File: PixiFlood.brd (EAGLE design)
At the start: 32 x 47.2 mm, 60 parts, among them IC1 74LVC1G125DBV, IC2 WS2811SOP8, IC3 BD9G401EFJ-ME2, IC4 AL-8861SOT89-5, IC5 AL-8861SOT89-5, IC6 AL-8861SOT89-5, Q1 BC847BC847, Q2 BC847BC847, Q3 BC847BC847

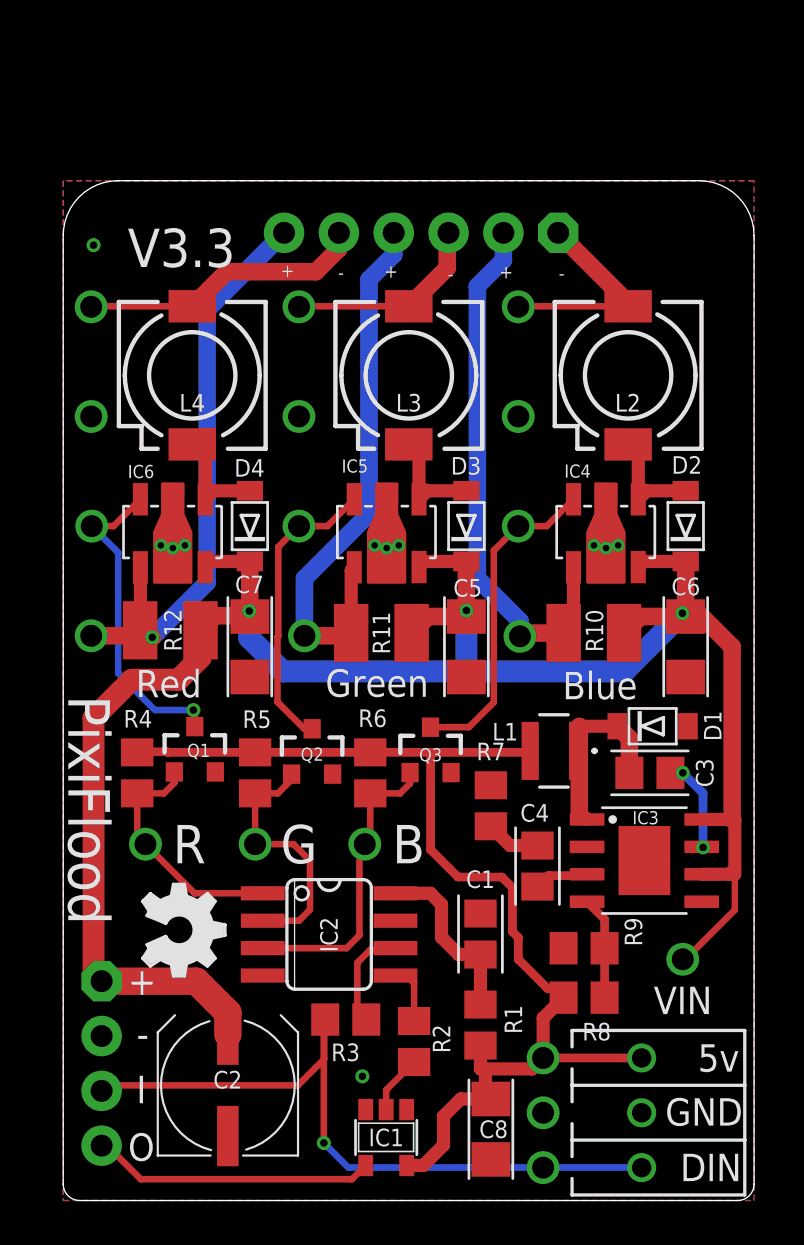
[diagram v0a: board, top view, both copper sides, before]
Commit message: Cleaned up some labels
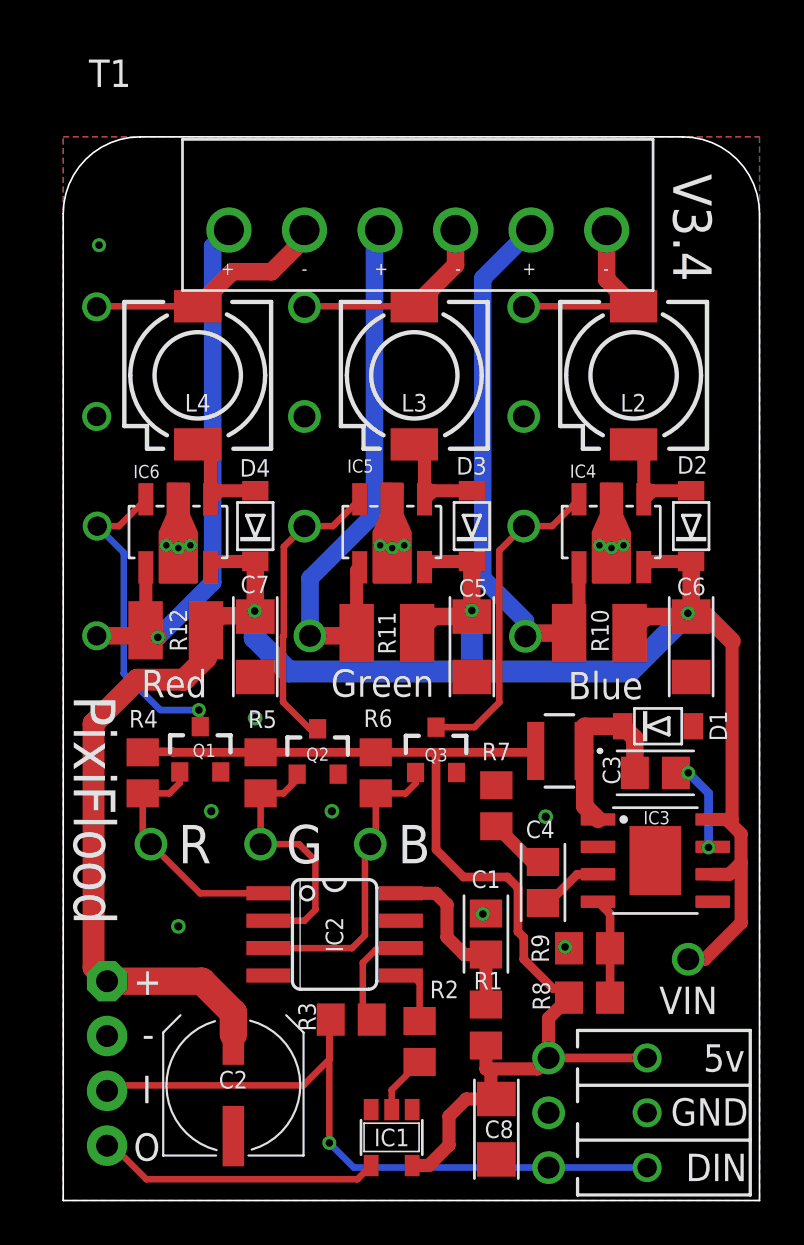
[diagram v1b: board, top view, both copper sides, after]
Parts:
- removed HDR3: (no value), headers:1X06
- added T1: ST06ECH350V-06P, connectors:ECH350V-06P
- LOGO: device ohw-logo:OSHW_FILLX150_NOTEXT -> ohw-logo:OSHW_FILLX200_NOTEXT
- TP1, TP14, TP4, TP9: device headers:TP-2 -> headers:TP-1
- moved LOGO 4.20 mm to (7.88, 10.3), turned to 0 degrees
- moved C4 0.80 mm to (22.2, 14.7)
- moved IC3 0.51 mm to (27.4, 15.7)
- moved C1 0.25 mm to (19.6, 12.3)
- moved C5 0.25 mm to (18.9, 25.7)
- moved C6 0.25 mm to (29.1, 25.7)
- moved D1 0.25 mm to (27.6, 22.0)
- moved D2 0.25 mm to (29.1, 31.2)
- moved D3 0.25 mm to (18.9, 31.2)
- moved IC1 0.25 mm to (15.2, 2.92)
- moved Q2 0.25 mm to (11.8, 20.8)
- moved R1 0.25 mm to (19.6, 8.13)
- moved R10 0.25 mm to (24.8, 26.3)
- moved R2 0.25 mm to (16.5, 7.37)
- moved R8 0.25 mm to (24.4, 9.40)
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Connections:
- net BOUT-N: now also T1.6; no longer HDR3.1
- net BOUT-P: now also T1.5; no longer HDR3.2
- net GOUT-N: now also T1.4; no longer HDR3.3
- net GOUT-P: now also T1.3; no longer HDR3.4
- net ROUT-N: now also T1.2; no longer HDR3.5
- net ROUT-P: now also T1.1; no longer HDR3.6
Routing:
- net ROUT-N: track 13.3 -> 11.3 mm
- net ROUT-P: track 27.3 -> 26.2 mm
- net BOUT-N: track 9.84 -> 9.15 mm
- net BOUT-P: track 25.3 -> 25.9 mm
- net N$1: track 2.56 -> 3.10 mm
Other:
- board size 32 x 47.2 mm -> 32.3 x 49.3 mm
- board text added: "V3.4"
- board text removed: "V3.3"

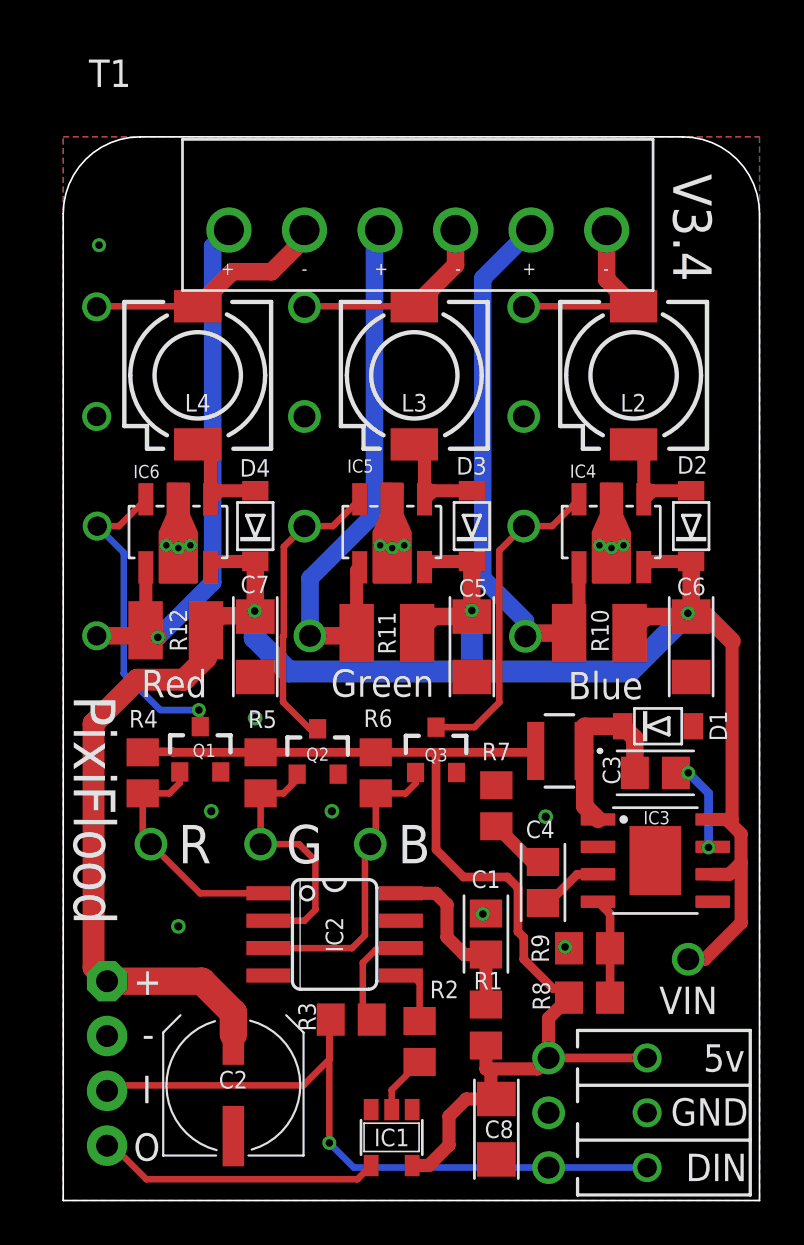
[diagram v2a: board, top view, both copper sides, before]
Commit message: Changed Connector
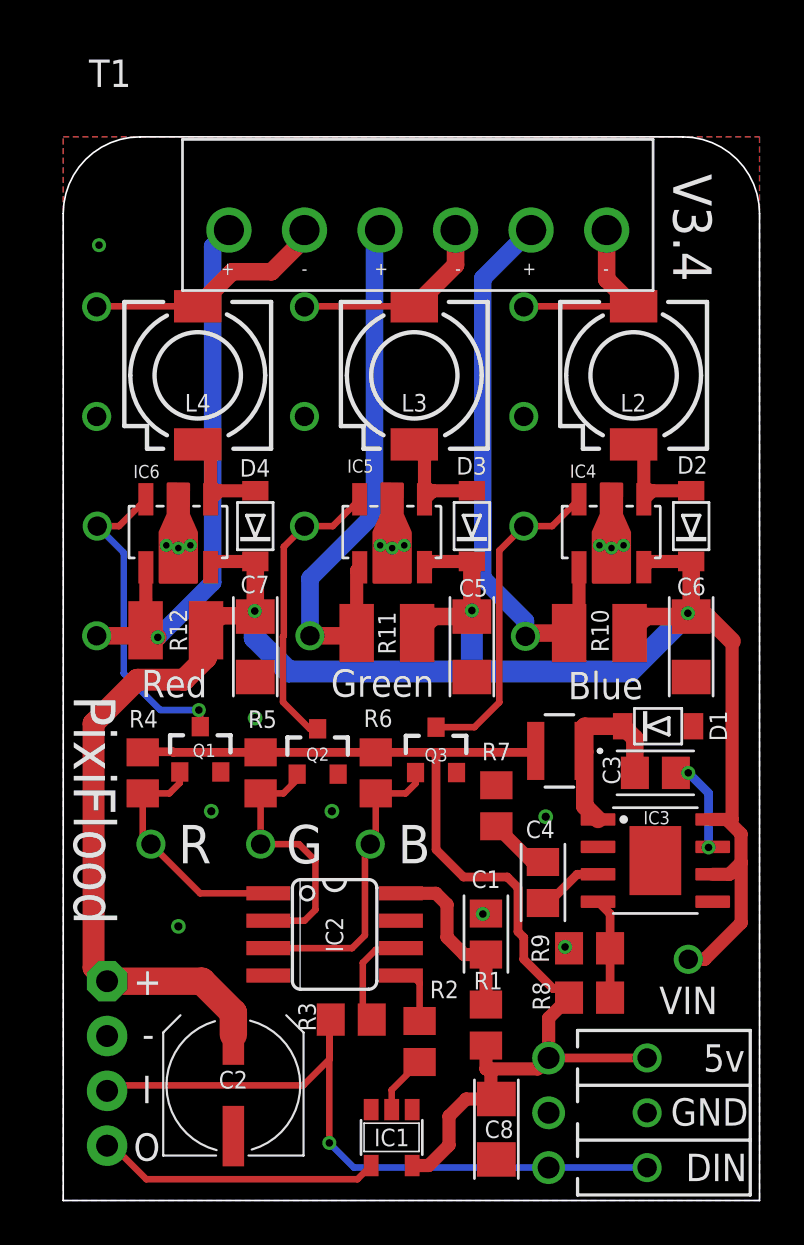
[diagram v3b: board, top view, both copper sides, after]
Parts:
- TP11, TP12, TP2, TP20, TP21, TP22, TP23, TP3, TP5, TP6, TP7, TP8: device headers:TP-2 -> headers:TP-1
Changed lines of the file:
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@@
 <attribute name="VALUE" x="5.588" y="7.501" size="0.6096" layer="27" rot="R180" align="center"/>
 </element>
-<element name="TP21" library="headers" package="TP-2" value="BIN" x="14.224" y="16.51" smashed="yes" rot="R90"/>
-<element name="TP22" library="headers" package="TP-2" value="GIN" x="9.144" y="16.51" smashed="yes" rot="R90"/>
+<element name="TP21" library="headers" package="TP-1" value="BIN" x="14.224" y="16.51" smashed="yes" rot="R90"/>
+<element name="TP22" library="headers" package="TP-1" value="GIN" x="9.144" y="16.51" smashed="yes" rot="R90"/>
 <element name="TP1" library="headers" package="TP-1" value="ROUT-N" x="1.5494" y="41.402" smashed="yes" rot="R180"/>
-<element name="TP2" library="headers" package="TP-2" value="GOUT-N" x="11.176" y="41.402" smashed="yes"/>
-<element name="TP3" library="headers" package="TP-2" value="BOUT-N" x="21.336" y="41.402" smashed="yes" rot="R180"/>
+<element name="TP2" library="headers" package="TP-1" value="GOUT-N" x="11.176" y="41.402" smashed="yes"/>
+<element name="TP3" library="headers" package="TP-1" value="BOUT-N" x="21.336" y="41.402" smashed="yes" rot="R180"/>
 <element name="R3" library="rcl" library_urn="urn:adsk.eagle:library:334" package="R0805" package3d_urn="urn:adsk.eagle:package:23553/2" value="33" x="13.343" y="8.382" smashed="yes">
 <attribute name="NAME" x="11.295" y="8.509" size="0.8128" layer="25" font="vector" ratio="10" rot="R270" align="center"/>
@@
 </element>
 <element name="TP4" library="headers" package="TP-1" value="RED" x="1.5748" y="31.242" smashed="yes" rot="R180"/>
-<element name="TP5" library="headers" package="TP-2" value="BLUE" x="21.336" y="31.242" smashed="yes" rot="R180"/>
-<element name="TP6" library="headers" package="TP-2" value="GREEN" x="11.176" y="31.242" smashed="yes" rot="R180"/>
-<element name="TP7" library="headers" package="TP-2" value="BOUT-P" x="21.4122" y="26.1366" smashed="yes"/>
-<element name="TP8" library="headers" package="TP-2" value="GOUT-P" x="11.43" y="26.162" smashed="yes"/>
+<element name="TP5" library="headers" package="TP-1" value="BLUE" x="21.336" y="31.242" smashed="yes" rot="R180"/>
+<element name="TP6" library="headers" package="TP-1" value="GREEN" x="11.176" y="31.242" smashed="yes" rot="R180"/>
+<element name="TP7" library="headers" package="TP-1" value="BOUT-P" x="21.4122" y="26.1366" smashed="yes"/>
+<element name="TP8" library="headers" package="TP-1" value="GOUT-P" x="11.43" y="26.162" smashed="yes"/>
 <element name="TP9" library="headers" package="TP-1" value="ROUT-R" x="1.5494" y="26.162" smashed="yes" rot="R180"/>
-<element name="TP11" library="headers" package="TP-2" value="RIN" x="4.064" y="16.51" smashed="yes" rot="R270"/>
-<element name="TP12" library="headers" package="TP-2" value="VIN" x="28.956" y="11.176" smashed="yes"/>
+<element name="TP11" library="headers" package="TP-1" value="RIN" x="4.064" y="16.51" smashed="yes" rot="R270"/>
+<element name="TP12" library="headers" package="TP-1" value="VIN" x="28.956" y="11.176" smashed="yes"/>
 <element name="R7" library="rcl" library_urn="urn:adsk.eagle:library:334" package="R0805" package3d_urn="urn:adsk.eagle:package:23553/2" value="4.7k" x="20.066" y="18.288" smashed="yes" rot="R270">
 <attribute name="NAME" x="20.066" y="20.8026" size="0.8128" layer="25" font="vector" ratio="10" align="center"/>
@@
 </element>
 <element name="TP19" library="headers" package="TP-1" value="GND" x="27.051" y="4.064" smashed="yes"/>
-<element name="TP20" library="headers" package="TP-2" value="GND" x="11.176" y="36.322" smashed="yes"/>
-<element name="TP23" library="headers" package="TP-2" value="GND" x="21.336" y="36.322" smashed="yes"/>
+<element name="TP20" library="headers" package="TP-1" value="GND" x="11.176" y="36.322" smashed="yes"/>
+<element name="TP23" library="headers" package="TP-1" value="GND" x="21.336" y="36.322" smashed="yes"/>
 <element name="TP13" library="headers" package="TP-1" value="DIN" x="27.051" y="1.524" smashed="yes"/>
 <element name="TP15" library="headers" package="TP-1" value="5V" x="27.051" y="6.604" smashed="yes"/>
@@
 <via x="22.352" y="17.78" extent="1-16" drill="0.381"/>
 <contactref element="IC1" pad="3"/>
-<wire x1="24.8412" y1="30.353" x2="21.336" y2="36.322" width="0" layer="19" extent="1-1"/>
-<wire x1="25.4" y1="30.226" x2="24.8412" y2="30.353" width="0" layer="19" extent="1-1"/>
-<wire x1="25.393975" y1="29.78688125" x2="25.4" y2="30.226" width="0" layer="19" extent="1-1"/>
-<wire x1="25.9588" y1="30.353" x2="25.4" y2="30.226" width="0" layer="19" extent="1-1"/>
-<wire x1="29.091" y1="24.254" x2="25.393975" y2="29.78688125" width="0" layer="19" extent="1-1"/>
-<wire x1="29.1965" y1="21.971" x2="29.091" y2="24.254" width="0" layer="19" extent="1-1"/>
-<wire x1="27.432" y1="15.748" x2="29.1965" y2="21.971" width="0" layer="19" extent="1-1"/>
-<wire x1="24.777" y1="16.383" x2="27.432" y2="15.748" width="0" layer="19" extent="1-1"/>
-<wire x1="22.352" y1="17.78" x2="24.777" y2="16.383" width="0" layer="19" extent="1-1"/>
-<wire x1="20.066" y1="19.238" x2="22.352" y2="17.78" width="0" layer="19" extent="1-1"/>
-<wire x1="18.222" y1="19.828" x2="20.066" y2="19.238" width="0" layer="19" extent="1-1"/>
-<wire x1="30.087" y1="13.843" x2="27.432" y2="15.748" width="0" layer="19" extent="1-1"/>
-<wire x1="18.931" y1="24.254" x2="18.222" y2="19.828" width="0" layer="19" extent="1-1"/>
-<wire x1="23.434" y1="11.684" x2="24.777" y2="16.383" width="0" layer="19" extent="1-1"/>
-<wire x1="23.249" y1="11.7475" x2="23.434" y2="11.684" width="0" layer="19" extent="1-1"/>
-<wire x1="19.5834" y1="13.2944" x2="23.249" y2="11.7475" width="0" layer="19" extent="1-1"/>
-<wire x1="19.439" y1="13.2715" x2="19.5834" y2="13.2944" width="0" layer="19" extent="1-1"/>
-<wire x1="12.7356" y1="19.7518" x2="18.222" y2="19.828" width="0" layer="19" extent="1-1"/>
-<wire x1="12.446" y1="18.034" x2="12.7356" y2="19.7518" width="0" layer="19" extent="1-1"/>
-<wire x1="8.89" y1="22.352" x2="12.7356" y2="19.7518" width="0" layer="19" extent="1-1"/>
-<wire x1="8.898" y1="24.254" x2="8.89" y2="22.352" width="0" layer="19" extent="1-1"/>
-<wire x1="7.3" y1="19.8534" x2="8.89" y2="22.352" width="0" layer="19" extent="1-1"/>
-<wire x1="6.858" y1="18.034" x2="7.3" y2="19.8534" width="0" layer="19" extent="1-1"/>
-<wire x1="5.334" y1="12.7" x2="6.858" y2="18.034" width="0" layer="19" extent="1-1"/>
-<wire x1="9.4996" y1="10.422" x2="5.334" y2="12.7" width="0" layer="19" extent="1-1"/>
-<wire x1="2.032" y1="7.62" x2="5.334" y2="12.7" width="0" layer="19" extent="1-1"/>
-<wire x1="5.327975" y1="29.78688125" x2="8.898" y2="24.254" width="0" layer="19" extent="1-1"/>
-<wire x1="5.334" y1="30.226" x2="5.327975" y2="29.78688125" width="0" layer="19" extent="1-1"/>
-<wire x1="5.8928" y1="30.353" x2="5.334" y2="30.226" width="0" layer="19" extent="1-1"/>
-<wire x1="4.7752" y1="30.353" x2="5.334" y2="30.226" width="0" layer="19" extent="1-1"/>
-<wire x1="15.233975" y1="29.78688125" x2="18.931" y2="24.254" width="0" layer="19" extent="1-1"/>
-<wire x1="15.24" y1="30.226" x2="15.233975" y2="29.78688125" width="0" layer="19" extent="1-1"/>
-<wire x1="15.7988" y1="30.353" x2="15.24" y2="30.226" width="0" layer="19" extent="1-1"/>
-<wire x1="14.6812" y1="30.353" x2="15.24" y2="30.226" width="0" layer="19" extent="1-1"/>
-<wire x1="1.5494" y1="36.322" x2="4.7752" y2="30.353" width="0" layer="19" extent="1-1"/>
-<wire x1="11.176" y1="36.322" x2="14.6812" y2="30.353" width="0" layer="19" extent="1-1"/>
-<wire x1="7.882" y1="2.984" x2="2.032" y2="7.62" width="0" layer="19" extent="1-1"/>
-<wire x1="14.26625" y1="4.211" x2="7.882" y2="2.984" width="0" layer="19" extent="1-1"/>
-<wire x1="16.16625" y1="4.211" x2="14.26625" y2="4.211" width="0" layer="19" extent="1-1"/>
-<wire x1="20.066" y1="1.902" x2="16.16625" y2="4.211" width="0" layer="19" extent="1-1"/>
-<wire x1="22.487" y1="4.064" x2="20.066" y2="1.902" width="0" layer="19" extent="1-1"/>
-<wire x1="27.051" y1="4.064" x2="22.487" y2="4.064" width="0" layer="19" extent="1-1"/>
-<wire x1="1.659" y1="44.2595" x2="1.5494" y2="36.322" width="0" layer="19" extent="1-1"/>
 </signal>
 <signal name="N$2">

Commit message: added adpater boards and changed pinout on led
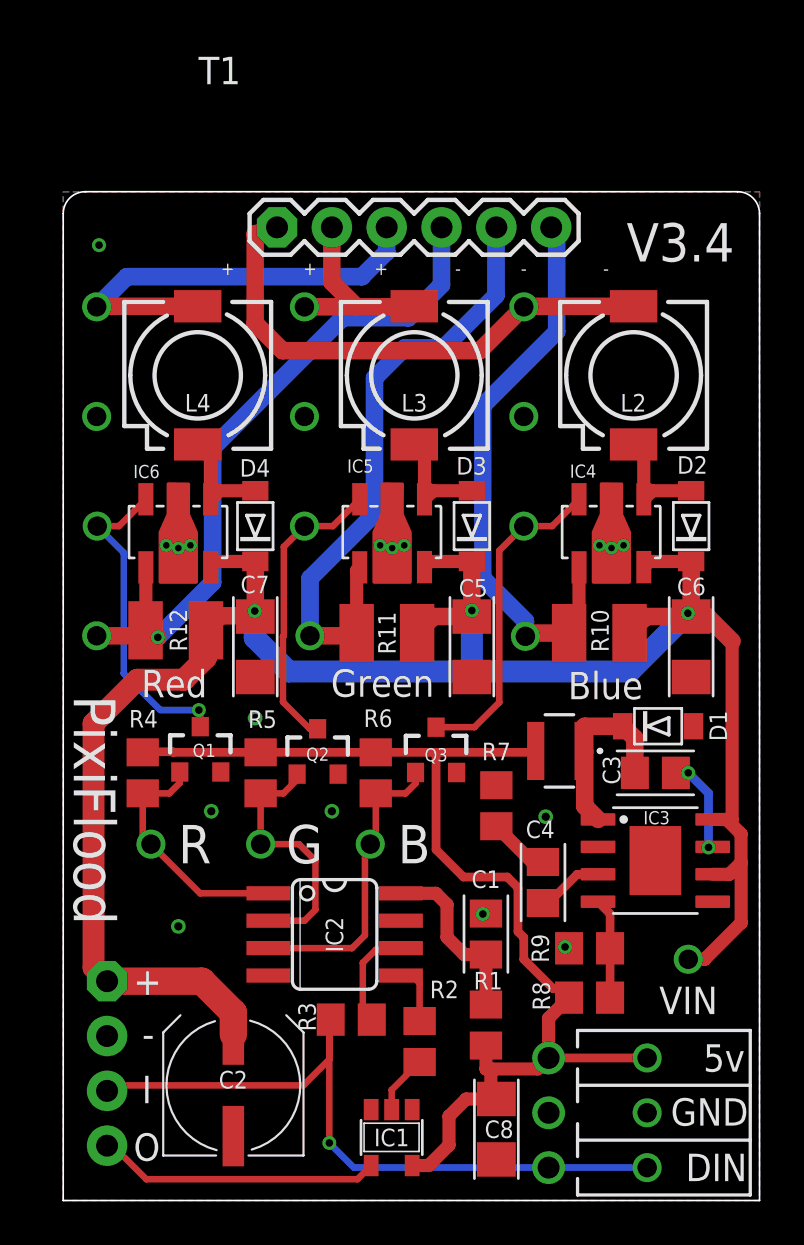
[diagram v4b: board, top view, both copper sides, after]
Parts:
- T1: value ST06ECH350V-06P -> (none); device connectors:ECH350V-06P -> headers:1X06
- moved T1 5.08 mm to (16.3, 45.1)
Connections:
- net BOUT-N: now also T1.1; no longer T1.6
- net BOUT-P: now also T1.6; no longer T1.5
- net GOUT-N: now also T1.2; no longer T1.4
- net GOUT-P: now also T1.5; no longer T1.3
- net ROUT-N: now also T1.3; no longer T1.2
- net ROUT-P: now also T1.4; no longer T1.1
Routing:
- net BOUT-N: track 9.15 -> 24.1 mm
- net ROUT-N: track 11.3 -> 20.3 mm
- net ROUT-P: track 26.2 -> 32.2 mm
- net GOUT-P: track 25.5 -> 28.9 mm
- net BOUT-P: track 25.9 -> 26.6 mm
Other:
- board size 32.3 x 49.3 mm -> 32.3 x 46.7 mm
